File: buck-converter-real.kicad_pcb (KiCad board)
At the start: 4 copper layers, 64 x 64 mm, 144 parts, among them J1 Conn_01x02_Pin, J1 USB_C_Receptacle_USB2.0_16P, J10 I2C1, J11 SWD, J12 Conn_01x04, J13 Conn_01x15, J14 Boot, J2 SOL 24V, J3 Battery out (3V6-4V2) NiMH 3S, J5 Barrel_Jack_MountingPin, J6 DM3CS-SF, J7 UART 1, J8 I2C1, J9 SWD, Q1 CSD18540Q5B - 60-V, SW2 SW_Omron_B3FS, U1 AP2112K-3.3 (3V3 LDO), U2 CH32V203K8T6, U5 LM5109BMA (Mosfet Driver), U6 78L12L (12V LDO) (35V max), Y1 8MHz 20pF

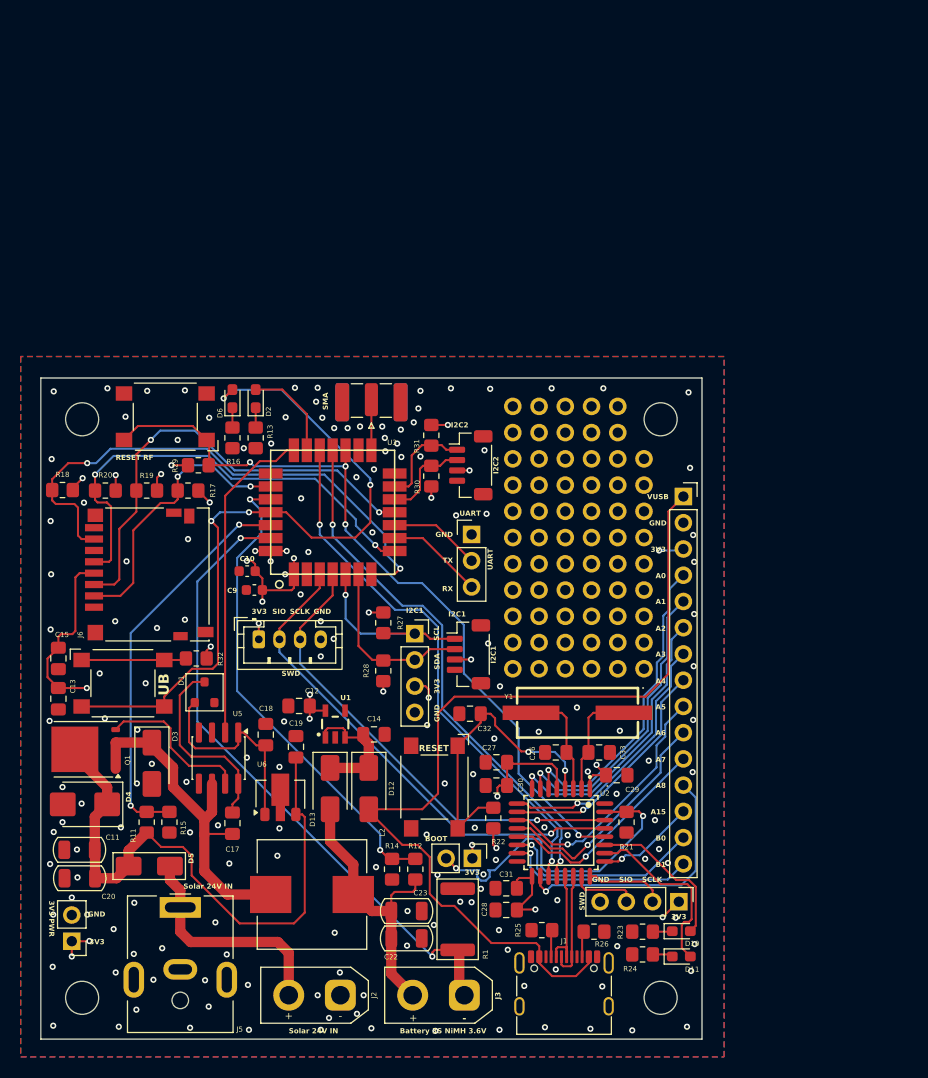
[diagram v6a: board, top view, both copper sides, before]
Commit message: Fix 3V3 to radio
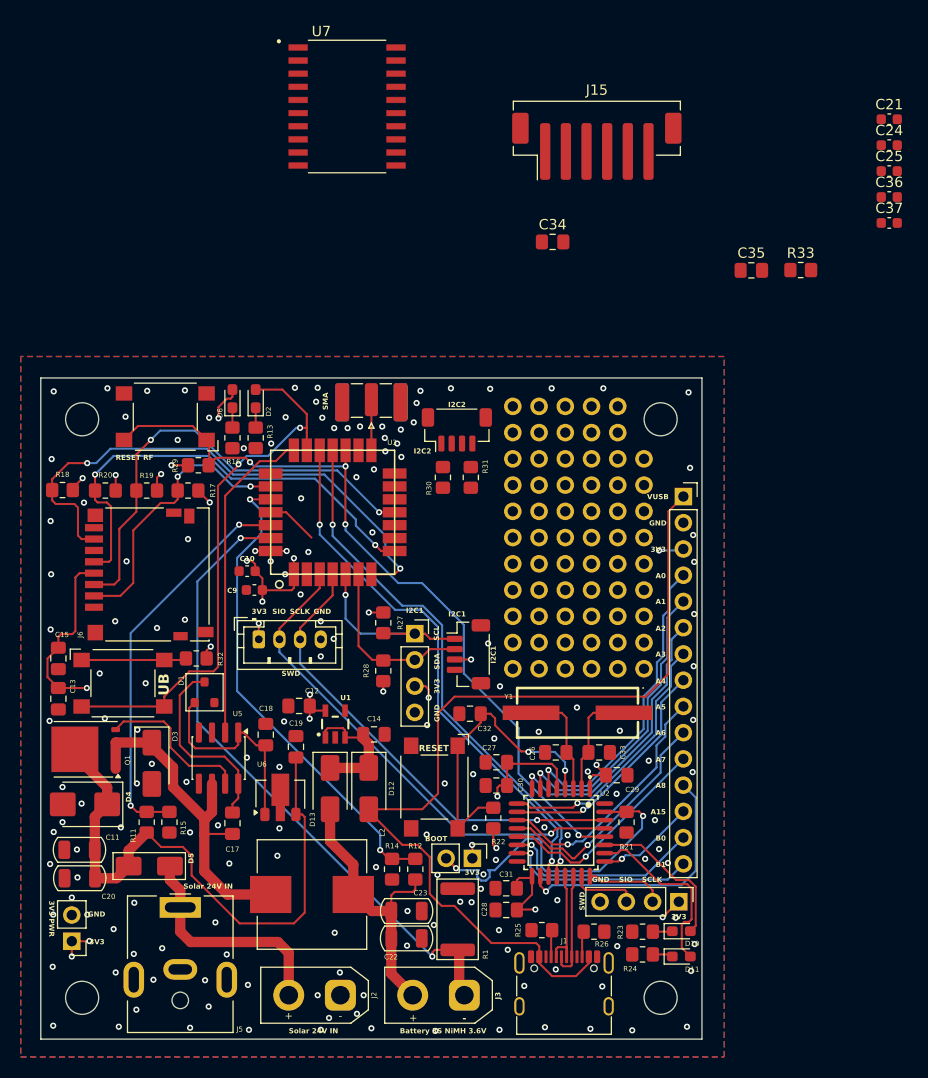
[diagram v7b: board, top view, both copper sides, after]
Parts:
- removed J7: UART 1, Connector_PinHeader_2.54mm:PinHeader_1x03_P2.54mm_Vertical
- added C21: 10uF 50V, Capacitor_SMD:C_0603_1608Metric, F.Cu at (150.1, 43.0)
- added C24: 1uF 50V, Capacitor_SMD:C_0603_1608Metric, F.Cu at (150.1, 45.5)
- added C25: 100nF 50V, Capacitor_SMD:C_0603_1608Metric, F.Cu at (150.1, 48.0)
- added C34: 10n 50V, Capacitor_SMD:C_0805_2012Metric_Pad1.18x1.45mm_HandSolder, F.Cu at (117.5, 54.8)
- added C35: 10n 50V, Capacitor_SMD:C_0805_2012Metric_Pad1.18x1.45mm_HandSolder, F.Cu at (136.8, 57.6)
- added C36: 1uF 50V, Capacitor_SMD:C_0603_1608Metric, F.Cu at (150.1, 50.5)
- added C37: 10uF 50V, Capacitor_SMD:C_0603_1608Metric, F.Cu at (150.1, 53.0)
- added J15: Conn_01x06, Connector_JST:JST_PH_B6B-PH-SM4-TB_1x06-1MP_P2.00mm_Vertical, F.Cu at (121.8, 45.6)
- added R33: 4.7K, Resistor_SMD:R_0805_2012Metric_Pad1.20x1.40mm_HandSolder, F.Cu at (141.6, 57.6)
- added U7: ISOW1432BDFMR, buck-forest:SOIC127P1030X355-20N, F.Cu at (97.7, 41.7)
- moved R31 5.59 mm to (109.6, 77.6), turned to 90 degrees
- moved J10 3.68 mm to (108.3, 73.0), turned to 0 degrees
- moved R30 1.13 mm to (106.9, 77.6)
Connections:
- D2 pad 1: Net-(D2-K) -> GND
- D2 pad 2: /LED2 -> Net-(D2-A)
- D6 pad 2: /LED1 -> +3.3V
- R13 pad 1: Net-(D2-K) -> GND
- RST2 pad 2: /LED1 -> Net-(D2-A)
- U3 pad 20: /LED2 -> Net-(D2-A)
- U3 pad 25: /LED1 -> /RS_EN
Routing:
- net /LED1: track 70.6 -> 0.00 mm, vias 4 -> 0
- net Net-(D2-A): track 0.00 -> 53.3 mm, vias 0 -> 2
- net /I2C-2-SCL: track 9.47 -> 0.00 mm
- net /UART-1-RX: track 9.41 -> 0.00 mm
- net /LED2: track 9.23 -> 0.00 mm
- net /UART-1-TX: track 8.87 -> 0.00 mm
- net /I2C-2-SCA: track 8.82 -> 0.00 mm
- net /RS_EN: track 0.00 -> 4.96 mm
- net Net-(D2-K): track 2.01 -> 0.00 mm
- net GND: track 0.00 -> 2.01 mm, vias 159 -> 155
- net +3.3V: track 93.3 -> 93.1 mm, vias 33 -> 31
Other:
- board text removed: "RX"
- board text removed: "TX"
- board text removed: "UART"

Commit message: Rearange, replace 12v ldo with buck
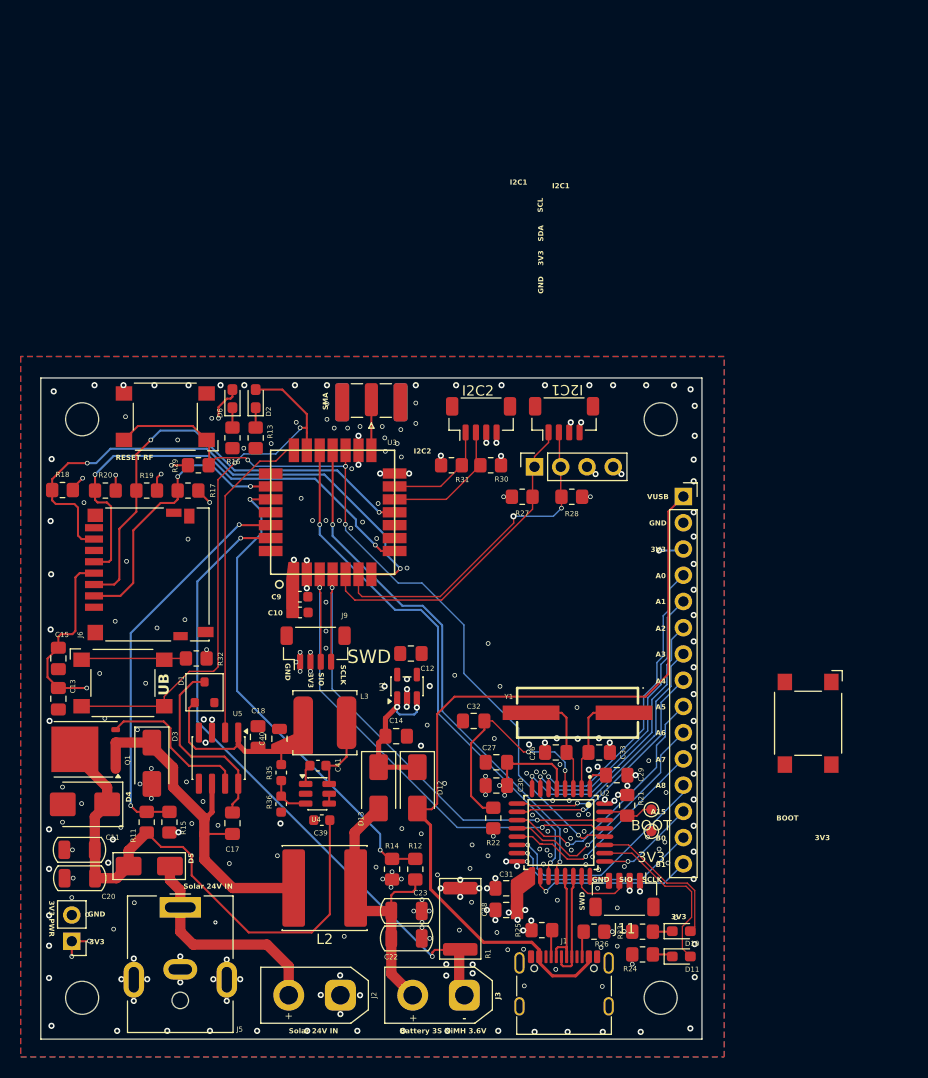
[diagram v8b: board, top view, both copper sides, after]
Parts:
- removed C19: 100nF 50V, Capacitor_SMD:C_0805_2012Metric_Pad1.18x1.45mm_HandSolder
- removed C21, C37: 10uF 50V, Capacitor_SMD:C_0603_1608Metric
- removed C24, C36: 1uF 50V, Capacitor_SMD:C_0603_1608Metric
- removed C25: 100nF 50V, Capacitor_SMD:C_0603_1608Metric
- removed C34, C35: 10n 50V, Capacitor_SMD:C_0805_2012Metric_Pad1.18x1.45mm_HandSolder
- removed J14: Boot, Connector_PinHeader_2.54mm:PinHeader_1x02_P2.54mm_Vertical
- removed J15: Conn_01x06, Connector_JST:JST_PH_B6B-PH-SM4-TB_1x06-1MP_P2.00mm_Vertical
- removed R33: 4.7K, Resistor_SMD:R_0805_2012Metric_Pad1.20x1.40mm_HandSolder
- removed REF**, REF**1, REF**10, REF**12, REF**13, REF**14, REF**15, REF**16, REF**17, REF**18, REF**19, REF**2, REF**20, REF**21, REF**22, REF**23, REF**24, REF**25, REF**26, REF**27, REF**28, REF**29, REF**3, REF**30, REF**31, REF**32, REF**33, REF**34, REF**35, REF**36, REF**37, REF**38, REF**39, REF**4, REF**40, REF**41, REF**42, REF**43, REF**44, REF**45, REF**46, REF**47, REF**48, REF**49, REF**50, REF**51, REF**52, REF**53, REF**54, REF**55, REF**56, REF**57, REF**58, REF**59, REF**6, REF**60, REF**61, REF**62, REF**63, REF**64, REF**65, REF**7, REF**8, REF**9: Untitled, forest-ch:Untitled
- removed U6: 78L12L (12V LDO) (35V max), Package_TO_SOT_SMD:SOT-89-3
- removed U7: ISOW1432BDFMR, buck-forest:SOIC127P1030X355-20N
- added C39: 2.2uF, Capacitor_SMD:C_0603_1608Metric, F.Cu at (95.2, 110.8)
- added C40: 15uF, Capacitor_SMD:C_0805_2012Metric, F.Cu at (91.1, 102.9)
- added C41: 100nF, Capacitor_SMD:C_0603_1608Metric, F.Cu at (94.8, 105.5)
- added L3: 56 uH, Inductor_SMD:L_TDK_VLS6045EX_VLS6045AF, F.Cu at (95.5, 101.4)
- added R35: 309, Capacitor_SMD:C_0603_1608Metric, F.Cu at (91.3, 106.2)
- added R36: 22.1, Capacitor_SMD:C_0603_1608Metric, F.Cu at (91.3, 109.2)
- added TP1: BOOT, TestPoint:TestPoint_Pad_D1.0mm, F.Cu at (127.1, 109.8)
- added TP2: 3V3, TestPoint:TestPoint_Pad_D1.0mm, F.Cu at (127.1, 111.9)
- added U4: LMR51603XDBVR, Package_TO_SOT_SMD:SOT-23-6, F.Cu at (94.8, 108.2)
- J11: footprint Connector_PinHeader_2.54mm:PinHeader_1x04_P2.54mm_Vertical -> Connector_JST:JST_SH_BM04B-SRSS-TB_1x04-1MP_P1.00mm_Vertical
- J9: footprint Connector_JST:JST_PH_B4B-PH-K_1x04_P2.00mm_Vertical -> Connector_JST:JST_SH_BM04B-SRSS-TB_1x04-1MP_P1.00mm_Vertical
- L2: footprint buck-forest:L_10.4x10.4_H4.8 -> Inductor_SMD:L_Sunlord_SWPA8040S
- U1: footprint PCM_SparkFun-Semiconductor-Standard:SOT23-5 -> Package_TO_SOT_SMD:SOT-23-5
- moved SW2 36.7 mm to (142.3, 101.4)
- moved R28 24.8 mm to (119.4, 79.5), turned to 180 degrees
- moved J8 24.6 mm to (118.7, 71.9), turned to 0 degrees
- moved J12 19.9 mm to (115.8, 76.6), turned to 90 degrees
- moved R27 18.2 mm to (114.6, 79.5), turned to 0 degrees
- moved C12 12.0 mm to (103.8, 94.7), turned to 0 degrees
- moved U1 7.85 mm to (103.5, 97.8)
- moved C10 6.50 mm to (93.1, 90.7), turned to 0 degrees
- moved J9 5.56 mm to (94.6, 94.1)
- moved J11 5.31 mm to (124.5, 118.0), turned to 180 degrees
- moved R30 4.77 mm to (111.5, 76.5), turned to 180 degrees
- moved D12 4.70 mm to (104.5, 107.7)
- moved D13 4.70 mm to (100.7, 107.7)
- moved C9 4.45 mm to (93.1, 89.2), turned to 0 degrees
- moved J10 2.58 mm to (110.6, 72.0)
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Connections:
- net /12V-OUT-LDO renamed /12V-buck
- D2 pad 1: GND -> Net-(D2-K)
- J10 pad MP: GND -> unconnected-(J10-Shield-PadMP)_1
- J11 pad 1: +3.3V -> GND
- J11 pad 2: /CH-SWD-CLK -> +3.3V
- J11 pad 4: GND -> /CH-SWD-CLK
- J8 pad MP: GND -> unconnected-(J8-Shield-PadMP)
- J9 pad 1: +3.3V -> GND
- J9 pad 2: /SWD-WIO-IO -> +3.3V
- J9 pad 3: /SWD-WIO-CLK -> /SWD-WIO-IO
- J9 pad 4: GND -> /SWD-WIO-CLK
- R13 pad 1: GND -> Net-(D2-K)
- U2 pad 14: Net-(J13-Pin_14) -> Net-(J13-Pin_12)
- U2 pad 15: Net-(J13-Pin_15) -> Net-(J13-Pin_14)
- U2 pad 18: Net-(J13-Pin_12) -> Net-(J13-Pin_15)
- U3 pad 28: +3.3V -> unconnected-(U3-VDD-Pad28)
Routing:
- net +3.3V: track 93.1 -> 50.6 mm, vias 31 -> 30
- net Net-(U2-PB8/BOOT0): track 32.7 -> 5.38 mm, vias 2 -> 0
- net /I2C-1-SDA: track 17.3 -> 33.0 mm, vias 0 -> 2
- net /I2C-1-SCL: track 18.5 -> 31.8 mm, vias 1 -> 0
- net /I2C-2-SCA: track 0.00 -> 13.0 mm
- net /I2C-2-SCL: track 0.00 -> 10.7 mm
- net VBUS: track 89.1 -> 81.5 mm
- net Net-(U4-SW): track 0.00 -> 7.58 mm
- net Net-(U2-NRST): track 29.1 -> 22.2 mm
- net /CH-SWD-CLK: track 7.70 -> 2.63 mm
- net /RS_EN: track 4.96 -> 0.00 mm
- net /12V-buck: track 20.3 -> 15.8 mm
- net /SWD-WIO-CLK: track 45.7 -> 50.0 mm, vias 1 -> 2
- net Net-(U4-FB): track 0.00 -> 4.18 mm
- net +BATT: track 27.6 -> 23.7 mm
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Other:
- board text removed: "RESET"
